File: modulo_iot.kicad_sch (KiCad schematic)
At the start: 49 parts, among them J3 SMA_CONNECTOR, Q10 BC817, Q11 BC817, Q2 BC817, Q3 BC817, Q4 BC817, Q5 BC817, Q6 BC817, Q7 BC817, Q8 BC817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

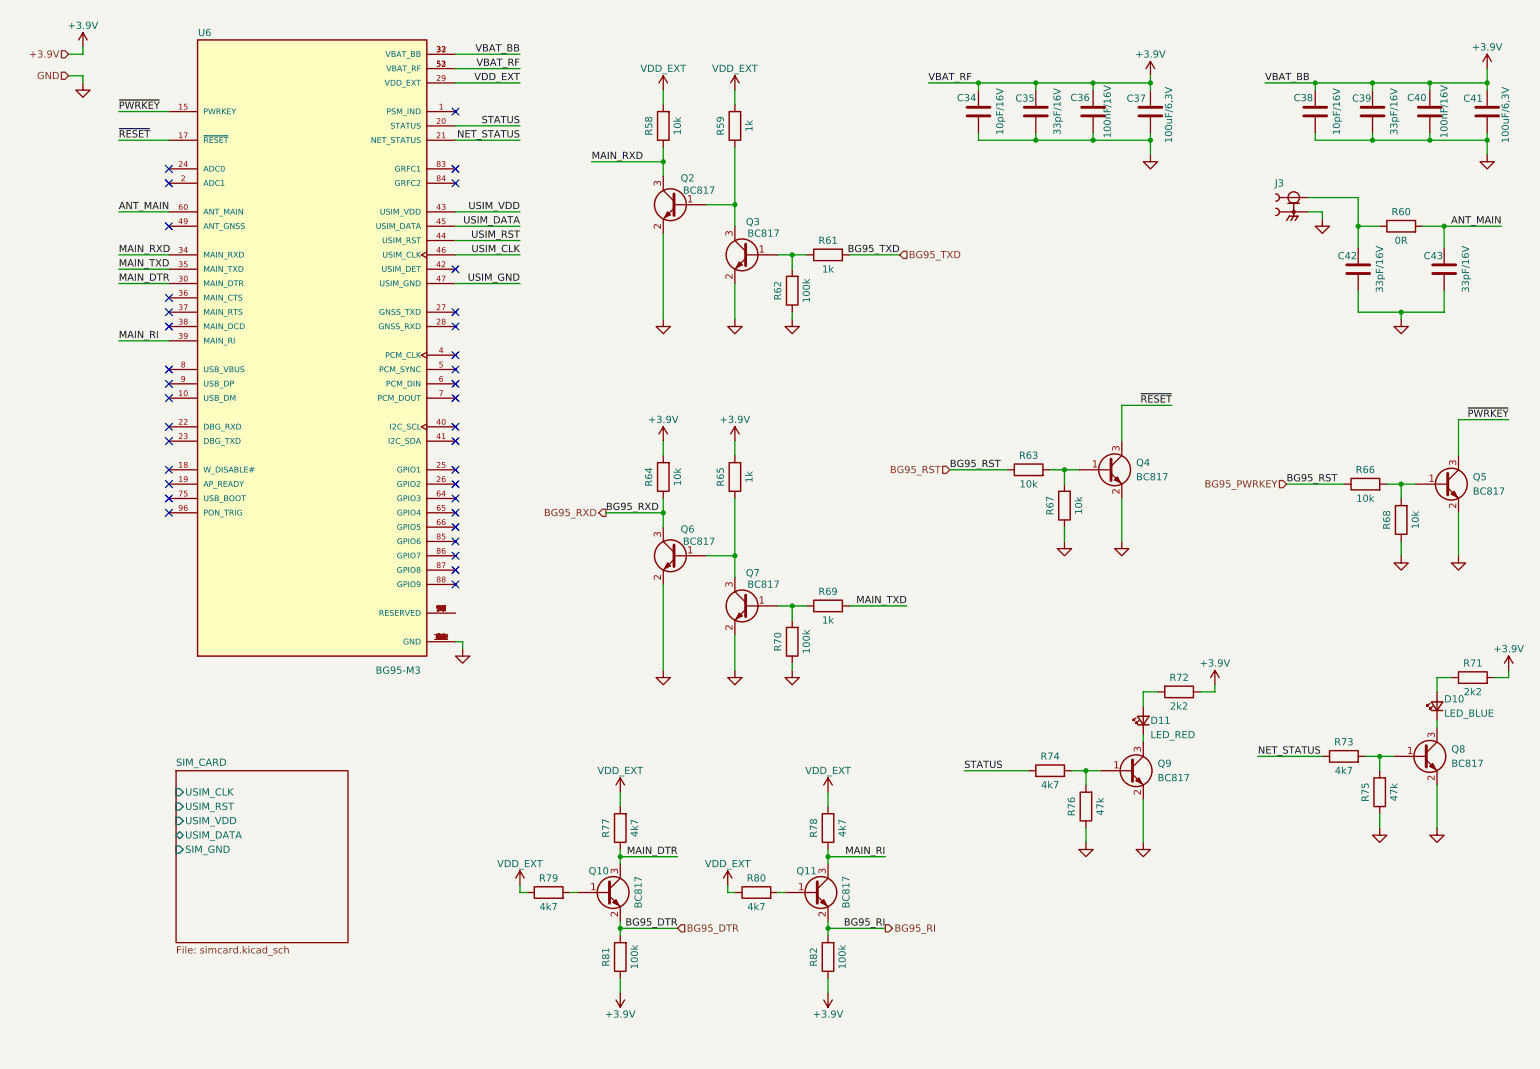
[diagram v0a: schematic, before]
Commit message: Atualização das referências dos componentes
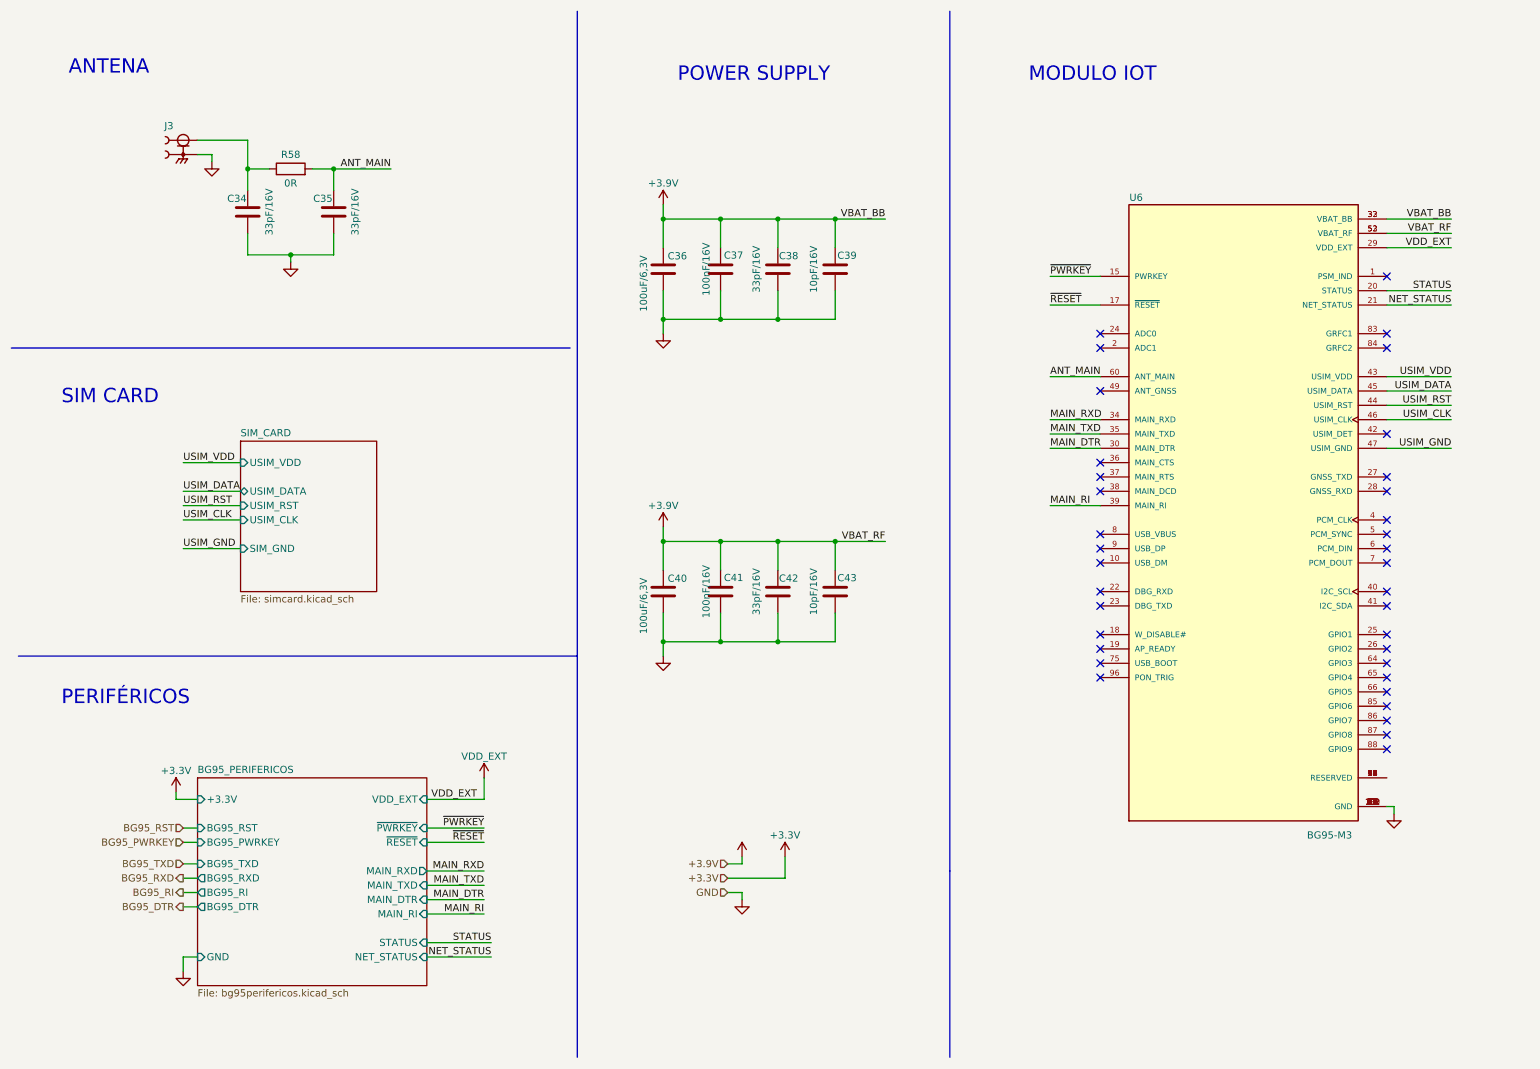
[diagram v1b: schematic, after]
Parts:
- removed C36: 100nF/16V, Capacitor_SMD:C_0402_1005Metric_Pad0.74x0.62mm_HandSolder, symbol Device:C
- removed C37: 100uF/6,3V, Capacitor_SMD:C_1206_3216Metric_Pad1.33x1.80mm_HandSolder, symbol Device:C
- removed D10: LED_BLUE, LED_SMD:LED_0603_1608Metric_Pad1.05x0.95mm_HandSolder, symbol Device:LED_Small
- removed D11: LED_RED, LED_SMD:LED_0603_1608Metric_Pad1.05x0.95mm_HandSolder, symbol Device:LED_Small
- removed Q10, Q11, Q2, Q3, Q4, Q5, Q6, Q7, Q8, Q9: BC817, Package_TO_SOT_SMD:SOT-23, symbol Transistor_BJT:BC817
- removed R59, R61, R65, R69: 1k, Resistor_SMD:R_0603_1608Metric_Pad0.98x0.95mm_HandSolder, symbol Device:R
- removed R60: 0R, Resistor_SMD:R_0603_1608Metric_Pad0.98x0.95mm_HandSolder, symbol Device:R
- removed R62, R70, R81, R82: 100k, Resistor_SMD:R_0603_1608Metric_Pad0.98x0.95mm_HandSolder, symbol Device:R
- removed R63, R64, R66, R67, R68: 10k, Resistor_SMD:R_0603_1608Metric_Pad0.98x0.95mm_HandSolder, symbol Device:R
- removed R71, R72: 2k2, Resistor_SMD:R_0603_1608Metric_Pad0.98x0.95mm_HandSolder, symbol Device:R
- removed R73, R74, R77, R78, R79, R80: 4k7, Resistor_SMD:R_0603_1608Metric_Pad0.98x0.95mm_HandSolder, symbol Device:R
- removed R75, R76: 47k, Resistor_SMD:R_0603_1608Metric_Pad0.98x0.95mm_HandSolder, symbol Device:R
- added C40: 100uF/6,3V, Capacitor_SMD:C_1206_3216Metric_Pad1.33x1.80mm_HandSolder, symbol Device:C
- added C41: 100nF/16V, Capacitor_SMD:C_0402_1005Metric_Pad0.74x0.62mm_HandSolder, symbol Device:C
- C34: value 10pF/16V -> 33pF/16V
- C43: value 33pF/16V -> 10pF/16V
- R58: value 10k -> 0R
- renumbered C41 to C36, C40 to C37, C39 to C38, C38 to C39
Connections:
- net ANT_MAIN: now also C35.2, R58.2; no longer C43.2
- net GND: now also C40.2, C41.1
- net MAIN_RXD: no longer R58.1
- net VBAT_RF: now also C42.2, C43.2, C40.1, C41.2; no longer C34.2, C35.2
- net at J3.1: now also C34.2, R58.1; no longer C42.2
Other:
- added sheet BG95_PERIFERICOS (bg95perifericos.kicad_sch)
- note added: "ANTENA"
- note added: "MODULO IOT"
- note added: "PERIFÉRICOS"
- note added: "POWER SUPPLY"
- note added: "SIM CARD"
- moved on the sheet: C36, C37, C38, C39, U6

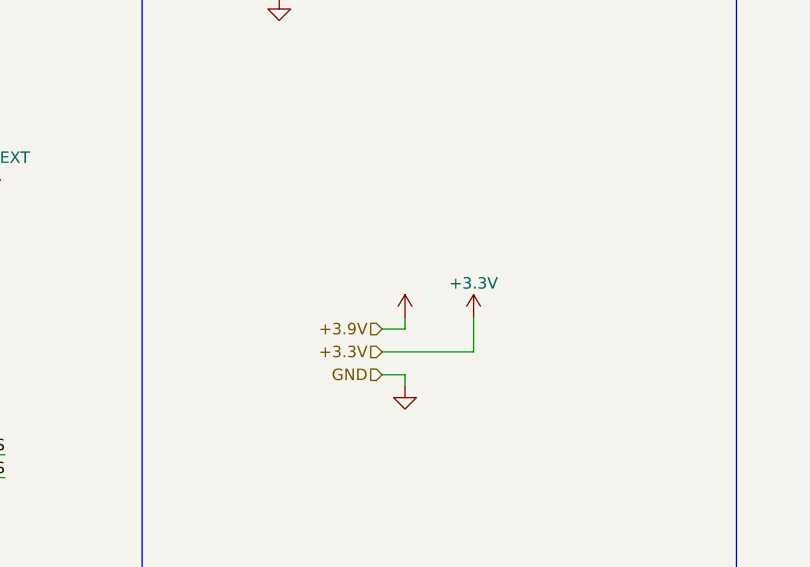
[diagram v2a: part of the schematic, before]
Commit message: Inserido as informações dos sheets do modulo IoT
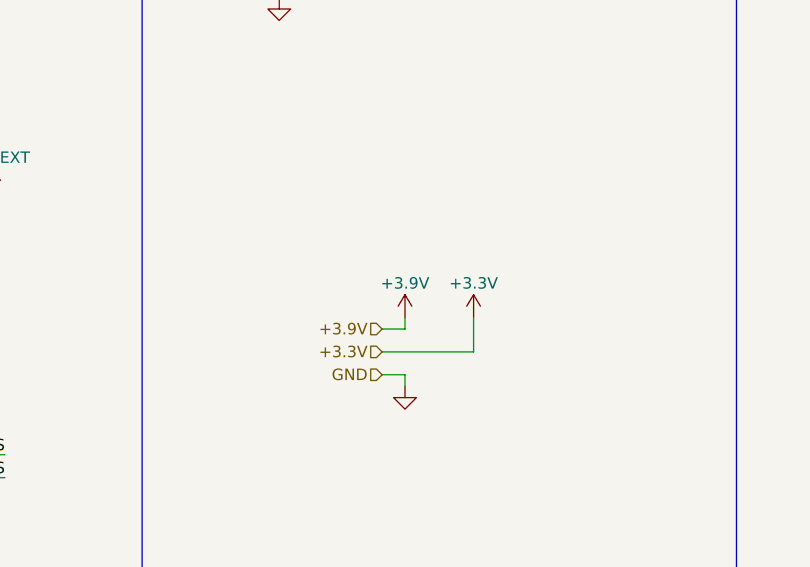
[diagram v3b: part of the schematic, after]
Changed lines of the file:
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@@
       (effects (font (size 1.27 1.27)) hide)
     )
-    (property "Value" "" (id 1) (at 139.7 158.75 0))
+    (property "Value" "+3.9V" (id 1) (at 139.7 158.75 0))
     (property "Footprint" "" (id 2) (at 139.7 162.56 0)
       (effects (font (size 1.27 1.27)) hide)

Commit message: Referencia dos componentes
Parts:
- renumbered R58 to R60
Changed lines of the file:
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@@
   (symbol (lib_id "Alexandre_Library:Power") (at 147.32 162.56 0) (unit 1)
     (in_bom yes) (on_board yes)
-    (property "Reference" "#PWR98" (id 0) (at 147.32 154.94 0)
+    (property "Reference" "#PWR99" (id 0) (at 147.32 154.94 0)
       (effects (font (size 1.27 1.27)) hide)
     )
@@
   (symbol (lib_id "Device:R") (at 59.69 40.64 90) (unit 1)
     (in_bom yes) (on_board yes)
-    (property "Reference" "R58" (id 0) (at 59.69 38.1 90))
+    (property "Reference" "R60" (id 0) (at 59.69 38.1 90))
     (property "Value" "0R" (id 1) (at 59.69 43.18 90))
     (property "Footprint" "Resistor_SMD:R_0603_1608Metric_Pad0.98x0.95mm_HandSolder" (id 2) (at 59.69 42.418 90)
@@
   (symbol (lib_id "power:GND") (at 255.27 154.94 0) (unit 1)
     (in_bom yes) (on_board yes) (fields_autoplaced)
-    (property "Reference" "#PWR096" (id 0) (at 255.27 161.29 0)
+    (property "Reference" "#PWR097" (id 0) (at 255.27 161.29 0)
       (effects (font (size 1.27 1.27)) hide)
     )
@@
   (symbol (lib_id "power:GND") (at 45.72 39.37 0) (unit 1)
     (in_bom yes) (on_board yes) (fields_autoplaced)
-    (property "Reference" "#PWR088" (id 0) (at 45.72 45.72 0)
+    (property "Reference" "#PWR089" (id 0) (at 45.72 45.72 0)
       (effects (font (size 1.27 1.27)) hide)
     )
@@
   (symbol (lib_id "power:GND") (at 125.73 127 0) (mirror y) (unit 1)
     (in_bom yes) (on_board yes) (fields_autoplaced)
-    (property "Reference" "#PWR093" (id 0) (at 125.73 133.35 0)
+    (property "Reference" "#PWR094" (id 0) (at 125.73 133.35 0)
       (effects (font (size 1.27 1.27)) hide)
     )
@@
   (symbol (lib_id "power:GND") (at 139.7 170.18 0) (unit 1)
     (in_bom yes) (on_board yes) (fields_autoplaced)
-    (property "Reference" "#PWR099" (id 0) (at 139.7 176.53 0)
+    (property "Reference" "#PWR0100" (id 0) (at 139.7 176.53 0)
       (effects (font (size 1.27 1.27)) hide)
     )
@@
   (symbol (lib_id "power:GND") (at 125.73 69.85 0) (mirror y) (unit 1)
     (in_bom yes) (on_board yes) (fields_autoplaced)
-    (property "Reference" "#PWR091" (id 0) (at 125.73 76.2 0)
+    (property "Reference" "#PWR092" (id 0) (at 125.73 76.2 0)
       (effects (font (size 1.27 1.27)) hide)
     )
@@
   (symbol (lib_id "Alexandre_Library:Power") (at 93.98 148.59 0) (unit 1)
     (in_bom yes) (on_board yes)
-    (property "Reference" "#PWR94" (id 0) (at 93.98 140.97 0)
+    (property "Reference" "#PWR95" (id 0) (at 93.98 140.97 0)
       (effects (font (size 1.27 1.27)) hide)
     )
@@
   (symbol (lib_id "power:GND") (at 40.64 182.88 0) (unit 1)
     (in_bom yes) (on_board yes) (fields_autoplaced)
-    (property "Reference" "#PWR0100" (id 0) (at 40.64 189.23 0)
+    (property "Reference" "#PWR0101" (id 0) (at 40.64 189.23 0)
       (effects (font (size 1.27 1.27)) hide)
     )
@@
   (symbol (lib_id "Alexandre_Library:Power") (at 39.37 151.13 0) (unit 1)
     (in_bom yes) (on_board yes)
-    (property "Reference" "#PWR95" (id 0) (at 39.37 143.51 0)
+    (property "Reference" "#PWR96" (id 0) (at 39.37 143.51 0)
       (effects (font (size 1.27 1.27)) hide)
     )
@@
   (symbol (lib_id "Alexandre_Library:Power") (at 139.7 162.56 0) (unit 1)
     (in_bom yes) (on_board yes)
-    (property "Reference" "#PWR97" (id 0) (at 139.7 154.94 0)
+    (property "Reference" "#PWR98" (id 0) (at 139.7 154.94 0)
       (effects (font (size 1.27 1.27)) hide)
     )
@@
   (symbol (lib_id "Alexandre_Library:Power") (at 125.73 104.14 0) (mirror y) (unit 1)
     (in_bom yes) (on_board yes)
-    (property "Reference" "#PWR92" (id 0) (at 125.73 96.52 0)
+    (property "Reference" "#PWR93" (id 0) (at 125.73 96.52 0)
       (effects (font (size 1.27 1.27)) hide)
     )
@@
   (symbol (lib_id "power:GND") (at 59.69 57.15 0) (unit 1)
     (in_bom yes) (on_board yes) (fields_autoplaced)
-    (property "Reference" "#PWR090" (id 0) (at 59.69 63.5 0)
+    (property "Reference" "#PWR091" (id 0) (at 59.69 63.5 0)
       (effects (font (size 1.27 1.27)) hide)
     )
@@
   (symbol (lib_id "Alexandre_Library:Power") (at 125.73 46.99 0) (mirror y) (unit 1)
     (in_bom yes) (on_board yes)
-    (property "Reference" "#PWR89" (id 0) (at 125.73 39.37 0)
-      (effects (font (size 1.27 1.27)) hide)
-    )
+    (property "Reference" "#PWR90" (id 0) (at 125.73 39.37 0)
+      (effects (font (size 1.27 1.27)) hide)
+    )

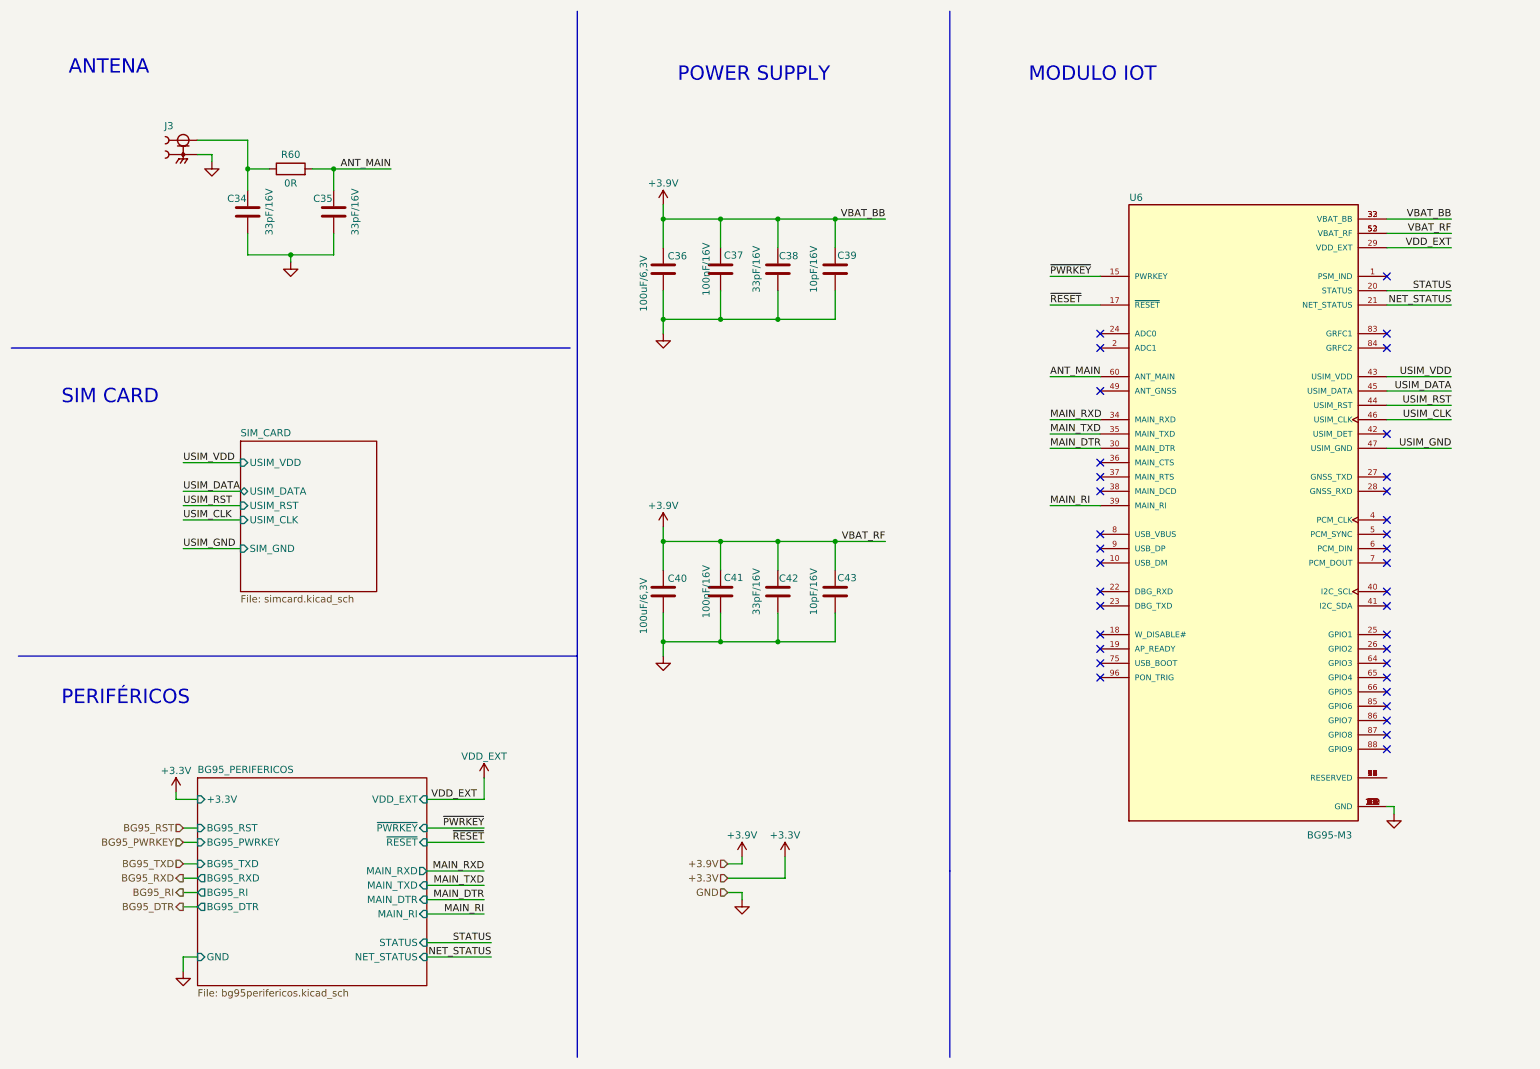
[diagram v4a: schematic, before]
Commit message: Inserido proteção ESD no SIM Card
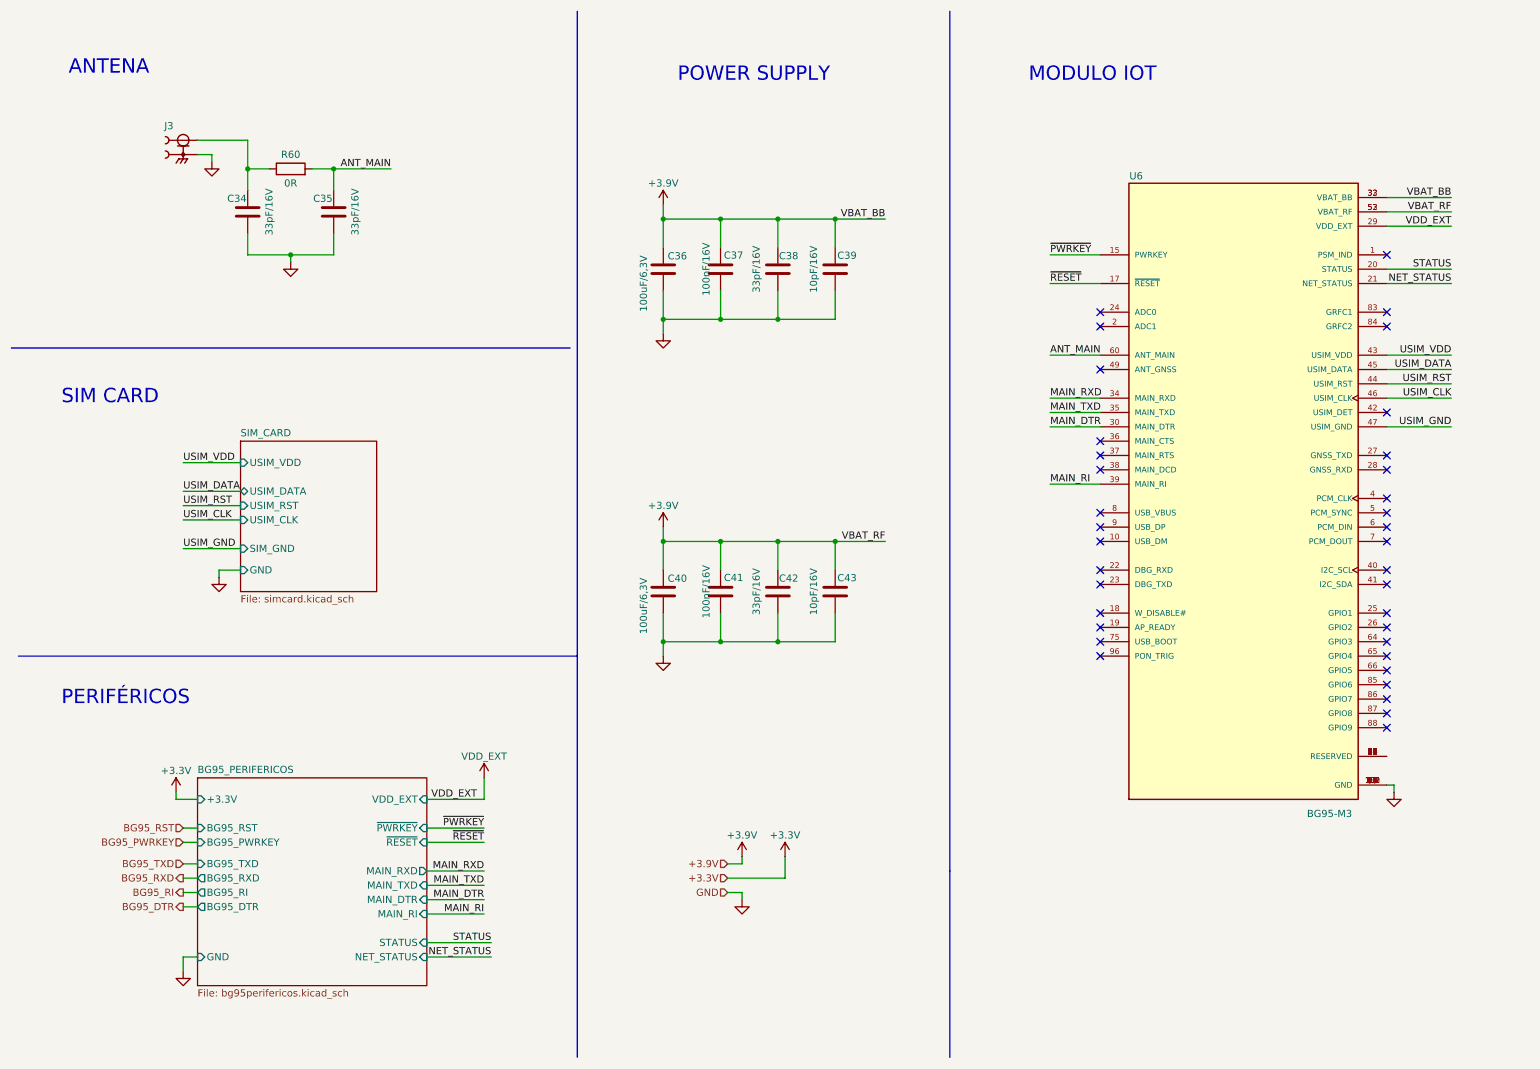
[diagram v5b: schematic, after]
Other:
- sheet SIM_CARD ports: added GND; removed none
- moved on the sheet: U6
